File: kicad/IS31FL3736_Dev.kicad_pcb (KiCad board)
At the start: 4 copper layers, 70.7 x 31.5 mm, 57 parts, among them J1 Daisy IN, J2 Daisy OUT, U1 IS31FL3736

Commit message: Board update
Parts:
- moved R1 11.5 mm to (130.4, 133.6), turned to 180 degrees
- moved R6 7.50 mm to (147.2, 141.2)
- moved R3 7.26 mm to (130.4, 136.1), turned to 180 degrees
- moved R5 4.82 mm to (130.4, 138.7), turned to 180 degrees
- moved U1 1.44 mm to (162.4, 141.3), turned to 180 degrees
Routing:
- net /SW8: track 0.00 -> 83.4 mm, vias 0 -> 8
- net /SW9: track 0.00 -> 81.6 mm, vias 0 -> 9
- net /SW5: track 0.00 -> 79.3 mm, vias 0 -> 9
- net /SW7: track 0.00 -> 77.5 mm, vias 0 -> 9
- net /SW6: track 0.00 -> 75.3 mm, vias 0 -> 9
- net /SW2: track 0.00 -> 73.8 mm, vias 0 -> 9
- net /SW4: track 0.00 -> 73.4 mm, vias 0 -> 9
- net /SW3: track 0.00 -> 70.8 mm, vias 0 -> 9
- net /SW1: track 0.00 -> 68.7 mm, vias 0 -> 8
- net /CS8: track 20.3 -> 0.00 mm
- net /CS6: track 20.1 -> 0.00 mm
- net /CS3: track 20.1 -> 0.00 mm
- net /CS2: track 20.1 -> 0.00 mm
- net /CS5: track 20.1 -> 0.00 mm
- net /CS1: track 20.1 -> 0.00 mm
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
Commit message: Layout done
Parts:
- removed C2, C3, C4: 0.47μF, Capacitor_SMD:C_0805_2012Metric
- added G***: LOGO, is31fl3736_dev:Address_Table, F.Cu at (151.1, 81.7)
- added G***: LOGO, is31fl3736_dev:MyBasic_rounded_50_1, F.Cu at (103.5, 75.9)
- added J3: Top_SW_Connector, Pin_Headers:Pin_Header_Straight_1x12_Pitch2.54mm, B.Cu at (160.5, 64.2)
- added J4: Bottom_CS_Connector, Pin_Headers:Pin_Header_Straight_1x08_Pitch2.54mm, F.Cu at (97.3, 76.4)
- added J5: Top_CS_Connector, Pin_Headers:Pin_Header_Straight_1x08_Pitch2.54mm, B.Cu at (97.4, 41.3)
- added REF**: MouseBites, is31fl3736_dev:MouseBites, F.Cu at (148.8, 69.0)
- added REF**: MouseBites, is31fl3736_dev:MouseBites, F.Cu at (127.6, 69.0)
- added REF**: MouseBites, is31fl3736_dev:MouseBites, F.Cu at (106.3, 69.0)
- added REF***: KiCad-Logo2_6mm_SilkScreen, Symbols:KiCad-Logo2_6mm_SilkScreen, F.Cu at (149.9, 95.7)
- J2: value Daisy OUT -> Bottom_SW_Connector; footprint Connector_PinHeader_2.54mm:PinHeader_1x09_P2.54mm_Horizontal -> Pin_Headers:Pin_Header_Straight_1x12_Pitch2.54mm; moved to F.Cu
- JP1, JP2, JP3, JP4, JP5, JP6, JP8: footprint Jumper:SolderJumper-2_P1.3mm_Open_Pad1.0x1.5mm -> Jumper:SolderJumper-2_P1.3mm_Open_RoundedPad1.0x1.5mm; moved to F.Cu
- JP7: value SLC ADDR2 -> SCL ADDR2; footprint Jumper:SolderJumper-2_P1.3mm_Open_Pad1.0x1.5mm -> Jumper:SolderJumper-2_P1.3mm_Open_RoundedPad1.0x1.5mm; moved to F.Cu
- R1, R2, R3, R4, R5: footprint Resistor_SMD:R_0805_2012Metric -> Resistors_SMD:R_0805
- R6: footprint Resistor_SMD:R_2512_6332Metric -> Resistors_SMD:R_0805
- U1: footprint Package_DFN_QFN:QFN-40-1EP_5x5mm_P0.4mm_EP3.8x3.8mm -> Housings_DFN_QFN:QFN-40-1EP_5x5mm_Pitch0.4mm
- moved C1 102.4 mm to (121.4, 74.6), turned to 180 degrees
- moved JP8 100.9 mm to (102.7, 87.8), turned to 180 degrees
- moved JP7 99.2 mm to (106.9, 87.8), turned to 180 degrees
- moved C7 98.7 mm to (125.2, 74.7), turned to 180 degrees
- moved C5 98.5 mm to (123.0, 78.8), turned to 90 degrees
- moved C6 92.0 mm to (123.0, 82.6), turned to 180 degrees
- moved JP4 91.2 mm to (102.7, 92.0), turned to 180 degrees
- moved JP6 89.8 mm to (111.5, 87.8), turned to 180 degrees
- moved JP3 89.6 mm to (106.9, 92.0), turned to 180 degrees
- moved JP5 88.5 mm to (115.7, 87.8), turned to 180 degrees
- moved C8 84.3 mm to (123.0, 87.6), turned to 180 degrees
- moved D15 82.6 mm to (126.3, 52.3), turned to 315 degrees
- moved D16 82.6 mm to (126.3, 57.8), turned to 315 degrees
- moved D19 82.6 mm to (133.5, 52.3), turned to 315 degrees
- moved D20 82.6 mm to (133.5, 57.8), turned to 315 degrees
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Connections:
- D1 pad 1: /SW11 -> /TSW11
- D1 pad 2: /SW10 -> /TSW10
- D1 pad 3: /SW12 -> /TSW12
- D1 pad 4: /CS1 -> /TCS1
- D10 pad 1: /SW8 -> /TSW8
- D10 pad 2: /SW7 -> /TSW7
- D10 pad 3: /SW9 -> /TSW9
- D10 pad 4: /CS3 -> /TCS3
- D11 pad 1: /SW5 -> /TSW5
- D11 pad 2: /SW4 -> /TSW4
- D11 pad 3: /SW6 -> /TSW6
- D11 pad 4: /CS3 -> /TCS3
- D12 pad 1: /SW2 -> /TSW2
- D12 pad 2: /SW1 -> /TSW1
- D12 pad 3: /SW3 -> /TSW3
- D12 pad 4: /CS3 -> /TCS3
- D13 pad 1: /SW11 -> /TSW11
- D13 pad 2: /SW10 -> /TSW10
- D13 pad 3: /SW12 -> /TSW12
- D13 pad 4: /CS4 -> /TCS4
- D14 pad 1: /SW8 -> /TSW8
- D14 pad 2: /SW7 -> /TSW7
- D14 pad 3: /SW9 -> /TSW9
- D14 pad 4: /CS4 -> /TCS4
- D15 pad 1: /SW5 -> /TSW5
- D15 pad 2: /SW4 -> /TSW4
- D15 pad 3: /SW6 -> /TSW6
- D15 pad 4: /CS4 -> /TCS4
- D16 pad 1: /SW2 -> /TSW2
- D16 pad 2: /SW1 -> /TSW1
- D16 pad 3: /SW3 -> /TSW3
- D16 pad 4: /CS4 -> /TCS4
- D17 pad 1: /SW11 -> /TSW11
- D17 pad 2: /SW10 -> /TSW10
- D17 pad 3: /SW12 -> /TSW12
- D17 pad 4: /CS5 -> /TCS5
- D18 pad 1: /SW8 -> /TSW8
- D18 pad 2: /SW7 -> /TSW7
- D18 pad 3: /SW9 -> /TSW9
- D18 pad 4: /CS5 -> /TCS5
- D19 pad 1: /SW5 -> /TSW5
- D19 pad 2: /SW4 -> /TSW4
- D19 pad 3: /SW6 -> /TSW6
- D19 pad 4: /CS5 -> /TCS5
- D2 pad 1: /SW8 -> /TSW8
- D2 pad 2: /SW7 -> /TSW7
- D2 pad 3: /SW9 -> /TSW9
- D2 pad 4: /CS1 -> /TCS1
- D20 pad 1: /SW2 -> /TSW2
- D20 pad 2: /SW1 -> /TSW1
- D20 pad 3: /SW3 -> /TSW3
- D20 pad 4: /CS5 -> /TCS5
- D21 pad 1: /SW11 -> /TSW11
- D21 pad 2: /SW10 -> /TSW10
- D21 pad 3: /SW12 -> /TSW12
- D21 pad 4: /CS6 -> /TCS6
- D22 pad 1: /SW8 -> /TSW8
- D22 pad 2: /SW7 -> /TSW7
- D22 pad 3: /SW9 -> /TSW9
- D22 pad 4: /CS6 -> /TCS6
- D23 pad 1: /SW5 -> /TSW5
- D23 pad 2: /SW4 -> /TSW4
- D23 pad 3: /SW6 -> /TSW6
- D23 pad 4: /CS6 -> /TCS6
- D24 pad 1: /SW2 -> /TSW2
- D24 pad 2: /SW1 -> /TSW1
- D24 pad 3: /SW3 -> /TSW3
- D24 pad 4: /CS6 -> /TCS6
- D25 pad 1: /SW11 -> /TSW11
- D25 pad 2: /SW10 -> /TSW10
- D25 pad 3: /SW12 -> /TSW12
- D25 pad 4: /CS7 -> /TCS7
- D26 pad 1: /SW8 -> /TSW8
- D26 pad 2: /SW7 -> /TSW7
- D26 pad 3: /SW9 -> /TSW9
- D26 pad 4: /CS7 -> /TCS7
- D27 pad 1: /SW5 -> /TSW5
- D27 pad 2: /SW4 -> /TSW4
- D27 pad 3: /SW6 -> /TSW6
- D27 pad 4: /CS7 -> /TCS7
- D28 pad 1: /SW2 -> /TSW2
- D28 pad 2: /SW1 -> /TSW1
- D28 pad 3: /SW3 -> /TSW3
- D28 pad 4: /CS7 -> /TCS7
- D29 pad 1: /SW11 -> /TSW11
- D29 pad 2: /SW10 -> /TSW10
- D29 pad 3: /SW12 -> /TSW12
- D29 pad 4: /CS8 -> /TCS8
- D3 pad 1: /SW5 -> /TSW5
- D3 pad 2: /SW4 -> /TSW4
- D3 pad 3: /SW6 -> /TSW6
- D3 pad 4: /CS1 -> /TCS1
- D30 pad 1: /SW8 -> /TSW8
- D30 pad 2: /SW7 -> /TSW7
- D30 pad 3: /SW9 -> /TSW9
- D30 pad 4: /CS8 -> /TCS8
- D31 pad 1: /SW5 -> /TSW5
- D31 pad 2: /SW4 -> /TSW4
- D31 pad 3: /SW6 -> /TSW6
- D31 pad 4: /CS8 -> /TCS8
- D32 pad 1: /SW2 -> /TSW2
- D32 pad 2: /SW1 -> /TSW1
- D32 pad 3: /SW3 -> /TSW3
- D32 pad 4: /CS8 -> /TCS8
- D4 pad 1: /SW2 -> /TSW2
- D4 pad 2: /SW1 -> /TSW1
- D4 pad 3: /SW3 -> /TSW3
- D4 pad 4: /CS1 -> /TCS1
- D5 pad 1: /SW11 -> /TSW11
- D5 pad 2: /SW10 -> /TSW10
- D5 pad 3: /SW12 -> /TSW12
- D5 pad 4: /CS2 -> /TCS2
- D6 pad 1: /SW8 -> /TSW8
- D6 pad 2: /SW7 -> /TSW7
- D6 pad 3: /SW9 -> /TSW9
- D6 pad 4: /CS2 -> /TCS2
- D7 pad 1: /SW5 -> /TSW5
- D7 pad 2: /SW4 -> /TSW4
- D7 pad 3: /SW6 -> /TSW6
- D7 pad 4: /CS2 -> /TCS2
- D8 pad 1: /SW2 -> /TSW2
- D8 pad 2: /SW1 -> /TSW1
- D8 pad 3: /SW3 -> /TSW3
- D8 pad 4: /CS2 -> /TCS2
- D9 pad 1: /SW11 -> /TSW11
- D9 pad 2: /SW10 -> /TSW10
- D9 pad 3: /SW12 -> /TSW12
- D9 pad 4: /CS3 -> /TCS3
- J1 pad 1: /DVCC -> /IICRST
- J1 pad 2: /Vio -> /~SDB
- J1 pad 3: /SDA -> /~INT_B
- J1 pad 5: /~INT_B -> /SDA
- J1 pad 6: /~SDB -> /SYNC
- J1 pad 7: /SYNC -> /Vio
- J1 pad 8: /IICRST -> /DVCC
- J2 pad 1: /DVCC -> /BSW2
- J2 pad 2: /Vio -> /BSW1
- J2 pad 3: /SDA -> /BSW3
- J2 pad 4: /SCL -> /BSW5
- J2 pad 5: /~INT_B -> /BSW4
- J2 pad 6: /~SDB -> /BSW6
- J2 pad 7: /SYNC -> /BSW8
- J2 pad 8: /IICRST -> /BSW7
- J2 pad 9: GND -> /BSW9
- R4 pad 2: /IICRST -> /~SDB
- U1 pad 1: /SW1 -> /BSW1
- U1 pad 10: /SW9 -> /BSW9
- U1 pad 12: /SW10 -> /BSW10
- U1 pad 13: /SW11 -> /BSW11
- U1 pad 14: /SW12 -> /BSW12
- U1 pad 15: /CS1 -> /BCS1
- U1 pad 16: /CS2 -> /BCS2
- U1 pad 18: /CS3 -> /BCS3
- U1 pad 19: /CS4 -> /BCS4
- U1 pad 2: /SW2 -> /BSW2
- U1 pad 21: /CS5 -> /BCS5
- U1 pad 22: /CS6 -> /BCS6
- U1 pad 24: /CS7 -> /BCS7
- U1 pad 25: /CS8 -> /BCS8
- U1 pad 3: /SW3 -> /BSW3
- U1 pad 5: /SW4 -> /BSW4
- U1 pad 6: /SW5 -> /BSW5
- U1 pad 7: /SW6 -> /BSW6
- U1 pad 8: /SW7 -> /BSW7
- U1 pad 9: /SW8 -> /BSW8
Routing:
- net /TCS8: track 0.00 -> 86.3 mm, vias 0 -> 4
- net /SW11: track 86.0 -> 0.00 mm, vias 9 -> 0
- net /SW8: track 83.4 -> 0.00 mm, vias 8 -> 0
- net /SW12: track 82.5 -> 0.00 mm, vias 9 -> 0
- net /TCS7: track 0.00 -> 81.8 mm, vias 0 -> 5
- net /SW9: track 81.6 -> 0.00 mm, vias 9 -> 0
- net /SW5: track 79.3 -> 0.00 mm, vias 9 -> 0
- net /SW10: track 79.0 -> 0.00 mm, vias 8 -> 0
- net /SW7: track 77.5 -> 0.00 mm, vias 9 -> 0
- net /SW6: track 75.3 -> 0.00 mm, vias 9 -> 0
- net /SW2: track 73.8 -> 0.00 mm, vias 9 -> 0
- net /SW4: track 73.4 -> 0.00 mm, vias 9 -> 0
- net /TCS6: track 0.00 -> 72.4 mm, vias 0 -> 5
- net /SW3: track 70.8 -> 0.00 mm, vias 9 -> 0
- net /SW1: track 68.7 -> 0.00 mm, vias 8 -> 0
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- added copper zone on B.Cu, net GND
- removed copper zone on In2.Cu, net /Vio
- removed copper zone on In1.Cu, net GND
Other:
- board size 70.7 x 31.5 mm -> 67.7 x 67.6 mm
- copper layers 4 -> 2
- net class Default: clearance 0.2 -> 0.1524; trace_width 0.25 -> 0.1524; via_dia 0.8 -> 0.6858; via_drill 0.4 -> 0.3302
- net class LED added: clearance 0.1524, trace_width 0.1524, via_dia 0.508, via_drill 0.254
- rule pad_to_mask_clearance: 0.0508 -> 0
- rule trace_clearance: 0.2 -> 0.1524
- board text added: "ADDR1"
- board text added: "DVCC"
- board text added: "GND"
- board text added: "IIC Interface Address Table"
- board text added: "IIC Interface Addressing"
- board text added: "IICRST"
- board text added: "IS31FL3736 Test Board R 1.0"
- board text added: "Optional"
- board text added: "SCL"
- board text added: "SDA"
- board text added: "SDB"
- board text added: "SYNC"
- board text added: "Vcc"
- board text added: "Vio"
- board text added: "~INTB"

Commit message: Update
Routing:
- net /DVCC: track 45.8 -> 49.6 mm
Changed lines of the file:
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@@
     (thickness 1.6)
     (drawings 51)
-    (tracks 895)
+    (tracks 899)
     (zones 0)
     (modules 63)
@@
   (segment (start 121.669999 96.6) (end 117.019999 91.95) (width 0.1524) (layer F.Cu) (net 1))
   (segment (start 116.35 91.95) (end 116.35 87.75) (width 0.1524) (layer F.Cu) (net 1))
+  (segment (start 122.97 78.75) (end 123.04 78.75) (width 0.1524) (layer F.Cu) (net 1))
+  (segment (start 122.97 78.75) (end 124.11 78.75) (width 0.1524) (layer F.Cu) (net 1))
+  (segment (start 124.86 79.5) (end 126.45 79.5) (width 0.1524) (layer F.Cu) (net 1))
+  (segment (start 124.11 78.75) (end 124.86 79.5) (width 0.1524) (layer F.Cu) (net 1))
   (segment (start 124.2725 74.74) (end 124.28 74.74) (width 0.1524) (layer F.Cu) (net 2))
   (segment (start 124.28 74.74) (end 124.29 74.73) (width 0.1524) (layer F.Cu) (net 2))
@@
   (segment (start 124.2725 74.4325) (end 123.4 73.56) (width 0.3048) (layer F.Cu) (net 2))
   (segment (start 124.2725 74.74) (end 124.2725 74.4325) (width 0.3048) (layer F.Cu) (net 2))
-  (segment (start 122.97 77.8425) (end 123.7025 77.8425) (width 0.3048) (layer F.Cu) (net 2))
-  (via (at 124.52 78.66) (size 0.508) (drill 0.254) (layers F.Cu B.Cu) (net 2))
-  (segment (start 123.7025 77.8425) (end 124.52 78.66) (width 0.3048) (layer F.Cu) (net 2))
   (via (at 120.95 84.89) (size 0.508) (drill 0.254) (layers F.Cu B.Cu) (net 2))
   (segment (start 122.16 85.089998) (end 121.149998 85.089998) (width 0.3048) (layer F.Cu) (net 2))
@@
   (via (at 124.55 80.78) (size 0.508) (drill 0.254) (layers F.Cu B.Cu) (net 2))
   (via (at 130.66 86.27) (size 0.508) (drill 0.254) (layers F.Cu B.Cu) (net 2))
+  (via (at 124.611257 78.568743) (size 0.508) (drill 0.254) (layers F.Cu B.Cu) (net 2))
+  (segment (start 123.885014 77.8425) (end 124.611257 78.568743) (width 0.3048) (layer F.Cu) (net 2))
+  (segment (start 122.97 77.8425) (end 123.885014 77.8425) (width 0.3048) (layer F.Cu) (net 2))
   (segment (start 124.209999 94.05879) (end 129.24 89.028789) (width 0.1524) (layer B.Cu) (net 3))
   (segment (start 124.209999 96.6) (end 124.209999 94.05879) (width 0.1524) (layer B.Cu) (net 3))

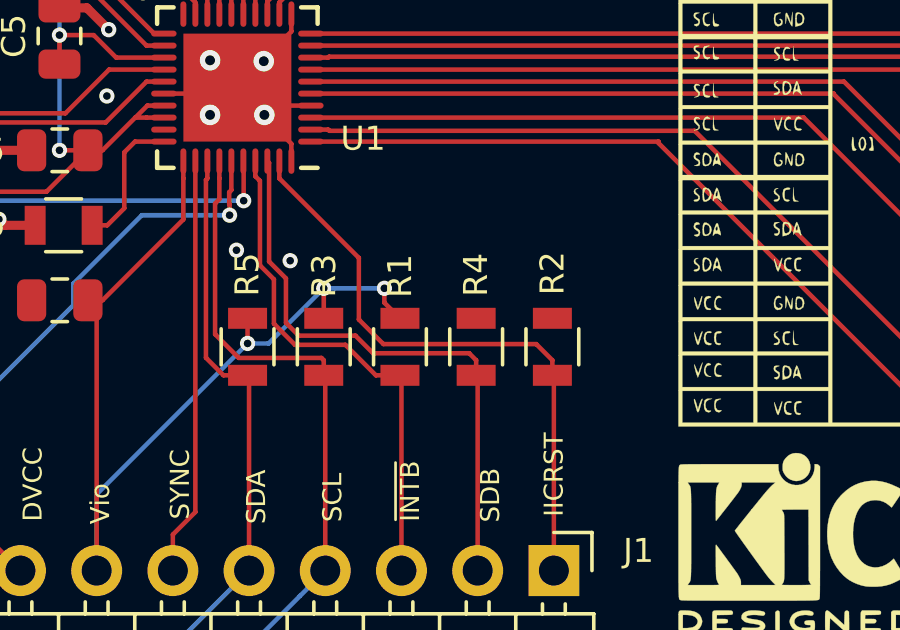
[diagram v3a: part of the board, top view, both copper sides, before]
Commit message: Update to SBD pullup
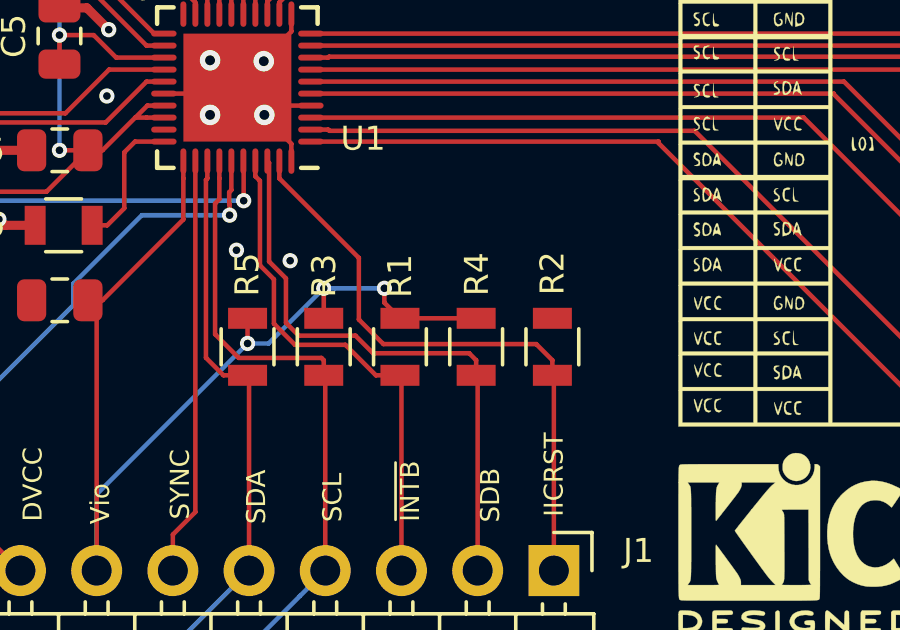
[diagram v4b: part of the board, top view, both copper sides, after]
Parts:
- J1: value Daisy IN -> I/O Connector
- turned R4 to 90 degrees
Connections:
- R4 pad 1: GND -> /~SDB
- R4 pad 2: /~SDB -> /Vio
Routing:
- net /Vio: track 33.4 -> 36.0 mm
